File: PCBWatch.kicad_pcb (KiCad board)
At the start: 2 copper layers, 62 x 40 mm, 36 parts, among them J1 Conn_01x05_Pin, J2 Touch Electrode, U1 STM32L010C6Tx, U2 MCP23017_SS, U3 AT42QT1010-TSHR, Y1 32.768KHZ

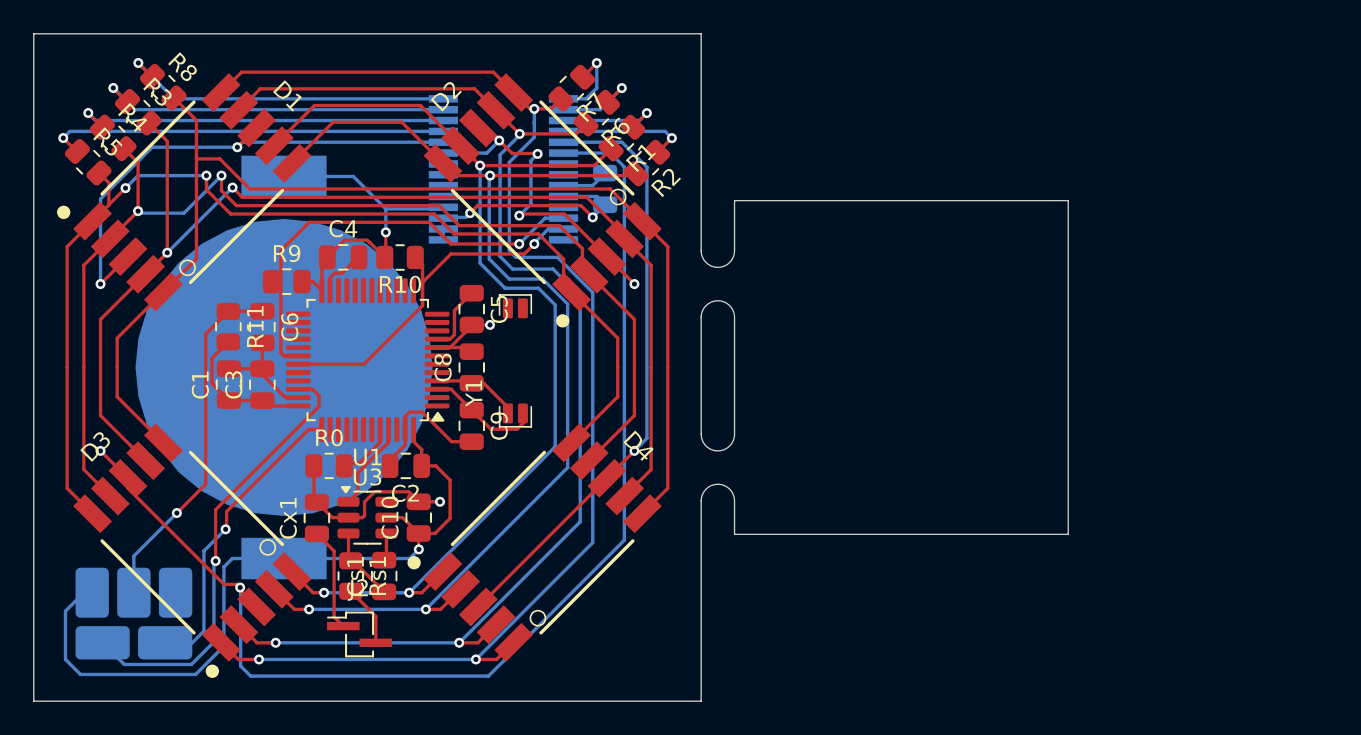
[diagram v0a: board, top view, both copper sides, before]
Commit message: Two level board
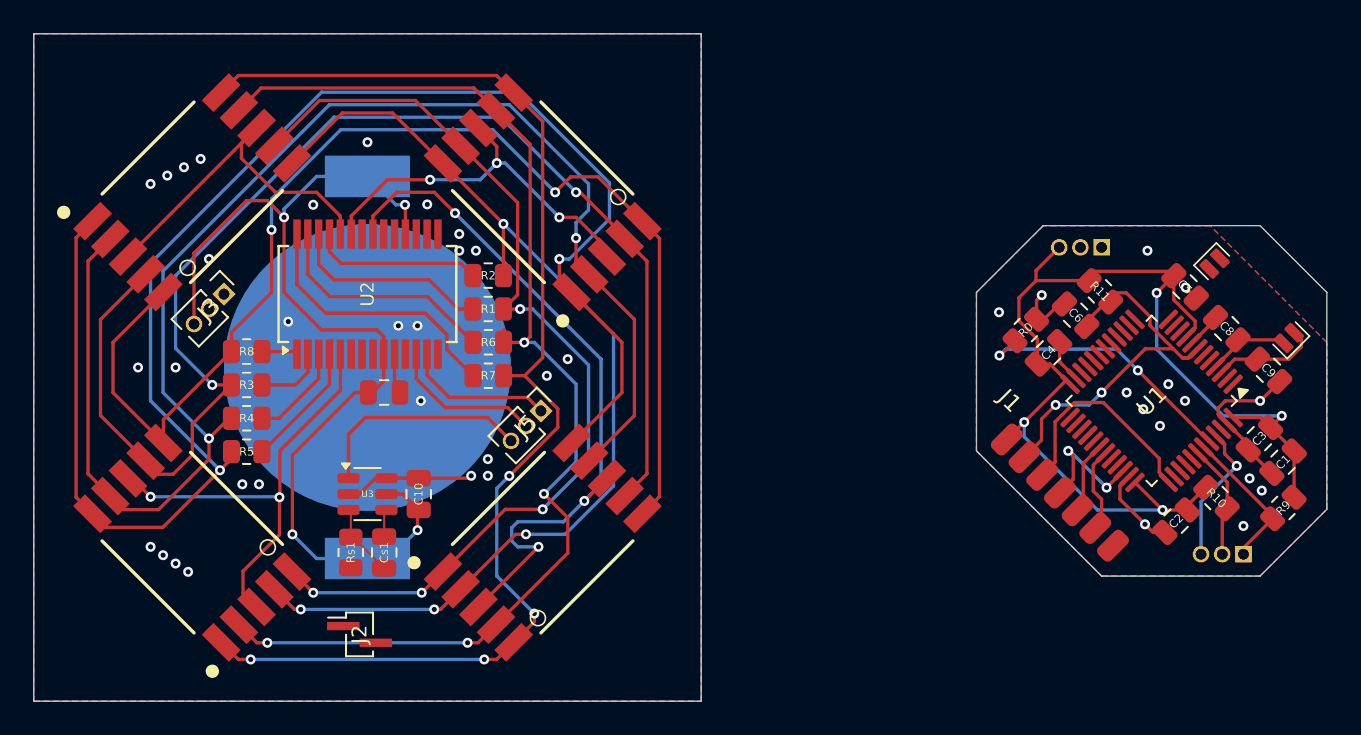
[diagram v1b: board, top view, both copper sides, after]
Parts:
- removed Cx1: 10p, Capacitor_SMD:C_0805_2012Metric
- added J3: Conn_A_left, Connector_PinHeader_1.27mm:PinHeader_1x03_P1.27mm_Vertical, F.Cu at (61.4, 90.6)
- added J4: Conn_B_left, my_footprints:3 Pin header socket, F.Cu at (112.7, 87.8)
- added J5: Conn_A_right, Connector_PinHeader_1.27mm:PinHeader_1x03_P1.27mm_Vertical, F.Cu at (80.4, 97.6)
- added J6: Conn_B_right, my_footprints:3 Pin header socket, F.Cu at (121.2, 106.2)
- C11, U2: moved to F.Cu
- J1: value Conn_01x05_Pin -> Conn_01x07_Pin; moved to F.Cu
- moved C1 63.3 mm to (124.9, 100.7), turned to -135 degrees
- moved R9 61.3 mm to (124.9, 103.4), turned to 45 degrees
- moved C3 59.8 mm to (123.5, 99.3), turned to -135 degrees
- moved J1 56.0 mm to (111.5, 102.5), turned to -45 degrees
- moved R11 52.3 mm to (113.9, 90.4), turned to 135 degrees
- moved R10 51.0 mm to (120.9, 102.8), turned to 135 degrees
- moved C6 48.7 mm to (112.4, 91.9), turned to 135 degrees
- moved C9 47.9 mm to (124.0, 95.2), turned to -45 degrees
- moved U1 47.0 mm to (117.0, 97.0), turned to -135 degrees
- moved Y1 46.7 mm to (124.9, 93.5), turned to 135 degrees
- moved C2 46.3 mm to (118.5, 104.2), turned to -135 degrees
- moved C8 45.3 mm to (121.5, 92.7), turned to 135 degrees
- moved C5 42.8 mm to (119.0, 90.2), turned to -45 degrees
- moved C4 42.7 mm to (110.8, 94.1), turned to 45 degrees
- moved R0 42.5 mm to (109.5, 92.8), turned to -135 degrees
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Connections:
- B1 pad 1: +3V0 -> +3V0-A
- B1 pad 2: GND -> GND-A
- C1 pad 1: +3V0 -> +3V0-B
- C1 pad 2: GND -> GND-B
- C10 pad 1: +3V0 -> +3V0-A
- C10 pad 2: GND -> GND-A
- C11 pad 1: +3V0 -> +3V0-A
- C11 pad 2: GND -> GND-A
- C2 pad 1: +3V0 -> +3V0-B
- C2 pad 2: GND -> GND-B
- C3 pad 1: +3V0 -> +3V0-B
- C3 pad 2: GND -> GND-B
- C4 pad 1: +3V0 -> +3V0-B
- C4 pad 2: GND -> GND-B
- C5 pad 1: +3V0 -> +3V0-B
- C5 pad 2: GND -> GND-B
- C6 pad 2: GND -> GND-B
- C8 pad 2: GND -> GND-B
- C9 pad 2: GND -> GND-B
- J1 pad 1: +3V0 -> +3V0-B
- J1 pad 2: /SWDIO -> /NRST
- J1 pad 4: /NRST -> /SWDIO
- J1 pad 5: GND -> /TX
- J2 pad 1: Net-(J2-Pin_1) -> unconnected-(J2-Pin_1-Pad1)
- R0 pad 1: GND -> GND-B
- R10 pad 1: /sda -> /sck-B
- R10 pad 2: +3V0 -> +3V0-B
- R11 pad 2: +3V0 -> +3V0-B
- R9 pad 1: /sck -> /sda-B
- R9 pad 2: +3V0 -> +3V0-B
- U1 pad 23: GND -> GND-B
- U1 pad 24: +3V0 -> +3V0-B
- U1 pad 30: /sck -> /TX
- U1 pad 31: /sda -> /RX
- U1 pad 35: GND -> GND-B
- U1 pad 36: +3V0 -> +3V0-B
- U1 pad 42: unconnected-(U1-PB6-Pad42) -> /sck-B
- U1 pad 43: unconnected-(U1-PB7-Pad43) -> /sda-B
- U1 pad 45: /touch -> /touch-B
- U1 pad 47: GND -> GND-B
- U1 pad 48: +3V0 -> +3V0-B
- U1 pad 8: GND -> GND-B
- U1 pad 9: +3V0 -> +3V0-B
- U2 pad 1: /row7-R -> /row8-R
- U2 pad 10: GND -> GND-A
- U2 pad 12: /sck -> /sck-A
- U2 pad 13: /sda -> /sda-A
- U2 pad 15: GND -> GND-A
- U2 pad 16: GND -> GND-A
- U2 pad 17: GND -> GND-A
- U2 pad 18: +3V0 -> +3V0-A
- U2 pad 2: /row6-R -> /row3-R
- U2 pad 21: unconnected-(U2-GPA0-Pad21) -> /column4
- U2 pad 25: /row5-R -> /row2-R
- U2 pad 26: /row4-R -> /row1-R
- U2 pad 27: /row3-R -> /row6-R
- U2 pad 28: /row8-R -> /row7-R
- U2 pad 3: /row1-R -> /row4-R
- U2 pad 4: /row2-R -> /row5-R
- U2 pad 5: /column4 -> /column3
- U2 pad 6: /column3 -> unconnected-(U2-GPB5-Pad6)
- U2 pad 9: +3V0 -> +3V0-A
- U3 pad 1: /touch -> /touch-A
- U3 pad 2: GND -> GND-A
- U3 pad 5: +3V0 -> +3V0-A
- U3 pad 6: unconnected-(U3-SYNC-Pad6) -> GND-A
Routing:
- net +3V0: track 81.4 -> 0.00 mm, vias 2 -> 0
- net +3V0-B: track 0.00 -> 67.7 mm, vias 0 -> 4
- net +3V0-A: track 0.00 -> 61.9 mm, vias 0 -> 4
- net GND: track 49.6 -> 0.00 mm, vias 4 -> 0
- net /column3: track 71.4 -> 27.5 mm
- net /row5: track 66.4 -> 97.3 mm
- net /sck: track 26.1 -> 0.00 mm, vias 1 -> 0
- net GND-B: track 0.00 -> 23.4 mm, vias 0 -> 14
- net /sda: track 23.2 -> 0.00 mm, vias 1 -> 0
- net /row4: track 68.4 -> 89.4 mm
- net /SWDIO: track 26.5 -> 7.60 mm, vias 1 -> 2
- net /row8-R: track 20.4 -> 2.17 mm, vias 1 -> 0
- net /row3-R: track 21.5 -> 4.16 mm, vias 1 -> 0
- net /row4-R: track 22.7 -> 5.86 mm, vias 1 -> 0
- net /row5-R: track 24.2 -> 7.54 mm, vias 1 -> 0
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- added copper zone on B.Cu, net GND-A
- added copper zone on F.Cu, net GND-A
- added copper zone on B.Cu, net GND-B
- added copper zone on F.Cu, net GND-B
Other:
- board size 62 x 40 mm -> 77.5 x 40 mm

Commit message: Push old changes of version 3
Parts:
- removed C10: 0.1u, Capacitor_SMD:C_0805_2012Metric
- removed Cs1: 20n, Capacitor_SMD:C_0805_2012Metric
- removed J2: Touch Electrode, Connector_PinSocket_1.00mm:PinSocket_1x02_P1.00mm_Vertical_SMD_Pin1Left
- removed Rs1: 2k2, Resistor_SMD:R_0805_2012Metric
- removed U3: AT42QT1010-TSHR, Package_TO_SOT_SMD:SOT-23-6
- added R12: 10K, Resistor_SMD:R_0805_2012Metric, F.Cu at (70.6, 102.5)
- added SW1: SW_SPST, my_footprints:SKQYAAE010 Switch, F.Cu at (70.0, 112.0)
- moved C1 15.9 mm to (110.9, 93.2)
- moved C2 15.9 mm to (104.5, 96.7)
- moved C3 15.9 mm to (109.5, 91.8)
- moved C4 15.9 mm to (96.8, 86.6)
- moved C5 15.9 mm to (105.0, 82.7)
- moved C6 15.9 mm to (98.4, 84.4)
- moved C8 15.9 mm to (107.5, 85.2)
- moved C9 15.9 mm to (110.0, 87.7)
- moved J1 15.9 mm to (97.5, 95.0)
- moved J4 15.9 mm to (98.7, 80.3)
- moved J6 15.9 mm to (107.2, 98.7)
- moved R0 15.9 mm to (95.5, 85.3)
- moved R10 15.9 mm to (106.9, 95.3)
- moved R11 15.9 mm to (99.9, 82.9)
- moved R9 15.9 mm to (110.9, 95.9)
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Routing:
- net GND-A: track 10.6 -> 2.54 mm, vias 28 -> 133
- net /touch-A: track 13.4 -> 19.3 mm
- net /row8: track 74.2 -> 79.5 mm
- net Net-(U3-SNSK): track 4.33 -> 0.00 mm
- net /row2: track 62.1 -> 59.5 mm
- net /column2: track 22.9 -> 25.4 mm
- net /row3: track 81.3 -> 83.6 mm
- net /column4: track 43.0 -> 41.1 mm
- net Net-(U3-SNS): track 1.66 -> 0.00 mm
- net GND-B: track 23.4 -> 25.1 mm
- net +3V0-A: track 61.9 -> 63.3 mm, vias 4 -> 3
- net /row6: track 70.7 -> 69.5 mm
- net /row1: track 58.9 -> 57.7 mm
- net /row7: track 75.9 -> 77.1 mm
- net /row5: track 97.3 -> 96.5 mm
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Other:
- board size 77.5 x 40 mm -> 64 x 40 mm
- board text added: "LED R"
- board text added: "PCBWatch"
- board text added: "PRESS"
- board text added: "rev. 3"

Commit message: E-ink first idea
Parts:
- removed D4: WL-S7DS, 7seg:WL-S7DS_0.3INCH
- removed J3: Conn_A_left, Connector_PinHeader_1.27mm:PinHeader_1x03_P1.27mm_Vertical
- removed J4: Conn_B_left, my_footprints:3 Pin header socket
- removed J5: Conn_A_right, Connector_PinHeader_1.27mm:PinHeader_1x03_P1.27mm_Vertical
- removed J6: Conn_B_right, my_footprints:3 Pin header socket
- removed R0, R11, R12: 10K, Resistor_SMD:R_0805_2012Metric
- removed R10, R9: 2k2, Resistor_SMD:R_0805_2012Metric
- removed R3, R4, R7, R8: 200, Resistor_SMD:R_0805_2012Metric
- removed SW1: SW_SPST, my_footprints:SKQYAAE010 Switch
- removed U2: MCP23017_SS, Package_SO:SSOP-28_5.3x10.2mm_P0.65mm
- added C10: 4u7, Capacitor_SMD:C_0805_2012Metric, B.Cu at (223.5, 35.0)
- added C12: 1u, Capacitor_SMD:C_0805_2012Metric, B.Cu at (210.5, 41.5)
- added C13: 1u, Capacitor_SMD:C_0805_2012Metric, B.Cu at (212.1, 38.5)
- added C14: 1u, Capacitor_SMD:C_0805_2012Metric, B.Cu at (211.4, 34.5)
- added C15: 1u, Capacitor_SMD:C_0805_2012Metric, B.Cu at (203.5, 30.9)
- added C16: 1u, Capacitor_SMD:C_0805_2012Metric, B.Cu at (208.5, 30.9)
- added C17: 1u(optional), Capacitor_SMD:C_0805_2012Metric, B.Cu at (212.1, 36.5)
- added C18: 1u, Capacitor_SMD:C_0805_2012Metric, B.Cu at (206.0, 30.9)
- added C19: 1u, Capacitor_SMD:C_0805_2012Metric, B.Cu at (210.5, 45.5)
- added C7: 0.1u, Capacitor_SMD:C_0805_2012Metric, B.Cu at (227.5, 38.0)
- added J2: E-Ink connector, 24-Pin-FPC-Connector:AMPHENOL_SFV24R-1STE1HLF, B.Cu at (206.0, 42.5)
- added L1: 10u, LQH32CN100K23L:IND_LQH32CN100K23L, B.Cu at (220.0, 35.6)
- added Q1: Si1304BDL / Si1308EDL TUBE MOS, Package_TO_SOT_SMD:SOT-323_SC-70_Handsoldering, B.Cu at (216.0, 33.7)
- added e-ink1: ~, E-Ink-1.54:E-Ink 1.54 Display, F.Cu at (206.2, 26.5)
- C1: value 10u -> 10p; moved to B.Cu
- C11: value 0.1u -> 1u; moved to B.Cu
- C2, C5, C6, J1, U1, Y1: moved to B.Cu
- C3: value 0.1u -> 10p; moved to B.Cu
- C4: value 0.1u -> 10u; moved to B.Cu
- C8: value 20p -> 0.1u; moved to B.Cu
- C9: value 20p -> 4u7; moved to B.Cu
- D1, D2, D3: value WL-S7DS -> MBR0530; footprint 7seg:WL-S7DS_0.3INCH -> Diode_SMD:D_SOD-123; moved to B.Cu
- R1, R2: value 200 -> 10K; moved to B.Cu
- R5: value 200 -> 10k; moved to B.Cu
- R6: value 200 -> 3/0.47; moved to B.Cu
- moved D3 175.2 mm to (217.5, 29.9), turned to -90 degrees
- moved R1 172.1 mm to (242.0, 41.9), turned to 90 degrees
- moved D1 171.9 mm to (222.5, 29.9), turned to -90 degrees
- moved R2 169.2 mm to (239.6, 41.9), turned to 90 degrees
- moved R5 166.0 mm to (216.1, 36.5)
- moved B1 161.3 mm to (224.5, 48.5), turned to 180 degrees
- moved C11 158.8 mm to (215.0, 29.6), turned to -90 degrees
- moved D2 149.8 mm to (220.0, 29.9), turned to -90 degrees
- moved C6 149.8 mm to (237.0, 27.5), turned to 180 degrees
- moved R6 149.3 mm to (216.1, 38.5), turned to 180 degrees
- moved J1 148.7 mm to (229.5, 26.5), turned to 180 degrees
- moved C2 146.6 mm to (242.0, 46.0), turned to -90 degrees
- moved C5 144.1 mm to (242.0, 38.0), turned to 90 degrees
- moved C1 142.9 mm to (239.6, 31.0), turned to 90 degrees
- moved C3 142.2 mm to (239.6, 34.5), turned to -90 degrees
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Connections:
- B1 pad 1: +3V0-A -> +3V0
- B1 pad 2: GND-A -> GND
- C1 pad 1: +3V0-B -> Net-(U1-PC14)
- C1 pad 2: GND-B -> GND
- C11 pad 1: +3V0-A -> /PREVGH
- C11 pad 2: GND-A -> GND
- C2 pad 1: +3V0-B -> /NRST
- C2 pad 2: GND-B -> GND
- C3 pad 1: +3V0-B -> Net-(U1-PC15)
- C3 pad 2: GND-B -> GND
- C4 pad 1: +3V0-B -> +3V0
- C4 pad 2: GND-B -> GND
- C5 pad 1: +3V0-B -> +3V0
- C5 pad 2: GND-B -> GND
- C6 pad 1: /NRST -> +3V0
- C6 pad 2: GND-B -> GND
- C8 pad 1: Net-(U1-PC15) -> +3V0
- C8 pad 2: GND-B -> GND
- C9 pad 1: Net-(U1-PC14) -> +3V0
- C9 pad 2: GND-B -> GND
- D1 pad 1: /row5 -> Net-(D1-K)
- D1 pad 2: /row4 -> /PREVGL
- D2 pad 1: /row5 -> GND
- D2 pad 2: /row4 -> Net-(D1-K)
- D3 pad 1: /row7 -> /PREVGH
- D3 pad 2: /row6 -> Net-(D3-A)
- J1 pad 1: +3V0-B -> +3V0
- J1 pad 7: GND-B -> GND
- R1 pad 1: /row1-R -> /NRST
- R1 pad 2: /row1 -> +3V0
- R2 pad 1: /row2-R -> GND
- R2 pad 2: /row2 -> Net-(U1-BOOT0)
- R5 pad 1: /row5-R -> GND
- R5 pad 2: /row5 -> /GDR
- R6 pad 1: /row6-R -> GND
- R6 pad 2: /row6 -> /RESE
- U1 pad 23: GND-B -> GND
- U1 pad 24: +3V0-B -> +3V0
- U1 pad 35: GND-B -> GND
- U1 pad 36: +3V0-B -> +3V0
- U1 pad 42: /sck-B -> /sck
- U1 pad 43: /sda-B -> /sda
- U1 pad 45: /touch-B -> unconnected-(U1-PB8-Pad45)
- U1 pad 47: GND-B -> GND
- U1 pad 48: +3V0-B -> +3V0
- U1 pad 8: GND-B -> GND
- U1 pad 9: +3V0-B -> +3V0
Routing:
- net /row5: track 96.5 -> 0.00 mm, vias 2 -> 0
- net +3V0: track 0.00 -> 89.8 mm, vias 0 -> 3
- net /row4: track 89.1 -> 0.00 mm, vias 2 -> 0
- net /row3: track 83.6 -> 0.00 mm, vias 2 -> 0
- net /row8: track 79.5 -> 0.00 mm, vias 2 -> 0
- net /row7: track 77.1 -> 0.00 mm, vias 4 -> 0
- net /row6: track 69.5 -> 0.00 mm, vias 4 -> 0
- net +3V0-B: track 67.7 -> 0.00 mm, vias 4 -> 0
- net +3V0-A: track 63.3 -> 0.00 mm, vias 3 -> 0
- net /row2: track 59.5 -> 0.00 mm, vias 4 -> 0
- net /row1: track 57.7 -> 0.00 mm, vias 4 -> 0
- net /column4: track 41.1 -> 0.00 mm, vias 3 -> 0
- net /PREVGL: track 0.00 -> 30.2 mm, vias 0 -> 2
- net /column3: track 27.5 -> 0.00 mm, vias 2 -> 0
- net GND: track 0.00 -> 26.5 mm, vias 0 -> 11
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- added copper zone on B.Cu, net GND
- added copper zone on F.Cu, net GND
- removed copper zone on B.Cu, net GND-A
- removed copper zone on F.Cu, net GND-A
- removed copper zone on B.Cu, net GND-B
- removed copper zone on F.Cu, net GND-B
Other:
- board size 64 x 40 mm -> 95 x 75 mm
- board text added: "rev. 4"
- board text removed: "LED R"
- board text removed: "PRESS"
- board text removed: "rev. 3"

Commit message: Semi-finished rev4 pcb
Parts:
- added J3: Pin header A, Connector_PinHeader_1.00mm:PinHeader_1x03_P1.00mm_Vertical, F.Cu at (201.5, 58.5)
- added J4: Pin header B, Connector_PinHeader_1.00mm:PinHeader_1x03_P1.00mm_Vertical, F.Cu at (201.5, 26.5)
- added J5: ~, PCB_USBC:PCBTypeC_14P, F.Cu at (228.2, 26.2)
- added J6: Pin header A top, Connector_PinHeader_1.00mm:PinHeader_1x03_P1.00mm_Vertical, F.Cu at (201.5, 95.5)
- added J7: Pin header B top, Connector_PinHeader_1.00mm:PinHeader_1x03_P1.00mm_Vertical, F.Cu at (201.5, 63.5)
- added R3: 100K, Resistor_SMD:R_0805_2012Metric, F.Cu at (202.5, 71.3)
- added R4: 100K, Resistor_SMD:R_0805_2012Metric, F.Cu at (202.5, 77.3)
- added R7: 100K, Resistor_SMD:R_0805_2012Metric, F.Cu at (202.5, 88.0)
- added S1: BUTTON, PTS526_SM15_SMTR2_LFS:PTS526SM15SMTR2LFS, F.Cu at (207.5, 71.2)
- added S2: BUTTON, PTS526_SM15_SMTR2_LFS:PTS526SM15SMTR2LFS, F.Cu at (207.5, 77.3)
- added S3: BUTTON, PTS526_SM15_SMTR2_LFS:PTS526SM15SMTR2LFS, F.Cu at (207.5, 87.8)
- J1: value Conn_01x07_Pin -> UART Pads; footprint my_footprints:SWD_pads -> my_footprints:Untitled_2
- L1: value 10u -> 10u/47u
- R6: value 3/0.47 -> 3/0.47/2.2
- moved C2 19.8 mm to (238.9, 26.4), turned to 0 degrees
- moved C4 16.0 mm to (243.0, 32.2), turned to 0 degrees
- moved J1 16.0 mm to (244.9, 30.8), turned to 90 degrees
- moved C7 15.7 mm to (242.9, 41.0), turned to 0 degrees
- moved R1 13.9 mm to (238.9, 28.4), turned to 0 degrees
- moved Y1 12.7 mm to (240.0, 45.5), turned to -90 degrees
- moved C1 12.5 mm to (242.0, 43.2), turned to 0 degrees
- moved C5 11.7 mm to (231.0, 34.0), turned to -90 degrees
- moved C14 10.3 mm to (202.0, 30.4), turned to 90 degrees
- moved C19 9.60 mm to (204.5, 53.0), turned to 180 degrees
- moved C3 8.82 mm to (238.5, 43.2), turned to 180 degrees
- moved C8 6.98 mm to (235.1, 43.2), turned to 0 degrees
- moved R2 5.60 mm to (243.5, 37.9)
- moved U1 5.12 mm to (237.3, 36.8), turned to 90 degrees
- moved C16 4.26 mm to (206.0, 27.5), turned to 180 degrees
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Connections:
- J1 pad 1: +3V0 -> /TX
- J1 pad 2: /NRST -> /RX
- J1 pad 3: /SWCLK -> GND
- J2 pad SH1: (no net) -> GND
- J2 pad SH2: (no net) -> GND
- U1 pad 11: unconnected-(U1-PA1-Pad11) -> /RES
- U1 pad 12: unconnected-(U1-PA2-Pad12) -> /BUSY
- U1 pad 13: unconnected-(U1-PA3-Pad13) -> /D/C
- U1 pad 14: unconnected-(U1-PA4-Pad14) -> /CS
- U1 pad 15: unconnected-(U1-PA5-Pad15) -> /SCLK
- U1 pad 17: unconnected-(U1-PA7-Pad17) -> /SDI
- U1 pad 20: unconnected-(U1-PB2-Pad20) -> /BUTTON1
- U1 pad 21: unconnected-(U1-PB10-Pad21) -> /BUTTON3
- U1 pad 22: unconnected-(U1-PB11-Pad22) -> /BUTTON2
- U1 pad 30: /TX -> unconnected-(U1-PA9-Pad30)
- U1 pad 31: /RX -> unconnected-(U1-PA10-Pad31)
- U1 pad 42: /sck -> /TX
- U1 pad 43: /sda -> /RX
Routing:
- net +3V0-T: track 0.00 -> 51.9 mm, vias 0 -> 6
- net /BUTTON2: track 0.00 -> 39.5 mm, vias 0 -> 1
- net /BUTTON1: track 0.00 -> 39.1 mm, vias 0 -> 1
- net /BUTTON3-T: track 0.00 -> 35.6 mm
- net +3V0: track 89.8 -> 125.1 mm, vias 3 -> 6
- net /BUTTON3: track 0.00 -> 35.1 mm, vias 0 -> 1
- net /RES: track 0.00 -> 30.0 mm, vias 0 -> 2
- net /BUSY: track 0.00 -> 28.2 mm, vias 0 -> 2
- net /SDI: track 0.00 -> 27.8 mm
- net /D/C: track 0.00 -> 27.6 mm
- net /SCLK: track 0.00 -> 27.0 mm
- net /CS: track 0.00 -> 26.9 mm
- net /BUTTON2-T: track 0.00 -> 26.7 mm, vias 0 -> 2
- net /BUTTON1-T: track 0.00 -> 20.8 mm, vias 0 -> 2
- net GND: track 26.5 -> 47.0 mm, vias 11 -> 53
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- added copper zone on B.Cu, net GND-T
- added copper zone on F.Cu, net GND-T
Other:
- board size 95 x 75 mm -> 45 x 73.2 mm
- board text added: "32.768 CRYSTAL"
- board text added: "A USB PORT"
- board text added: "CR2032 3V"
- board text added: "CS"
- board text added: "G"
- board text added: "MODE"
- board text added: "PCBWATCH REV4 TOMEK ZEBROWSKI"
- board text added: "PLUS"
- board text added: "RX"
- board text added: "SCK"
- board text added: "SDI"
- board text added: "SET"
- board text added: "SWD CONNECTOR"
- board text added: "THIS IS NOT"
- board text added: "TX"
- board text added: "USE HIGH PRECISION"
- board text added: "and bone. How can you"
- board text added: "challenge a perfect,"
- board text added: "immortal machine?"
- board text added: "look at you, hacker, a"
- board text added: "pathetic creature of meat"
- board text removed: "PCBWatch"
- board text removed: "rev. 4"
